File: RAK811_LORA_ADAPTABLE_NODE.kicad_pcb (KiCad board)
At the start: 2 copper layers, 75 x 49 mm, 41 parts, among them J1 Screw_Terminal_01x02, J10 Conn_01x01_Male, J11 Conn_01x01_Male, J12 Conn_01x01_Male, J13 Conn_01x01_Male, J14 Conn_01x01_Male, J15 Conn_01x01_Male, J16 Conn_01x01_Male, J17 Conn_01x01_Male, J18 Conn_01x01_Male, J19 Conn_01x01_Male, J2 Screw_Terminal_01x03, J20 Conn_01x01_Male, J21 Conn_01x01_Male, J22 Conn_01x01_Male, J23 Conn_01x01_Male, J24 Conn_01x01_Male, J25 Conn_01x01_Male, J26 Conn_01x01_Male, J27 Conn_01x01_Male, J28 Conn_01x01_Male, J29 Conn_01x01_Male, J3 Conn_01x01_Male, J30 Conn_01x01_Male, J31 Conn_01x01_Male, J32 Conn_01x01_Male, J4 Conn_01x01_Male, J5 Conn_01x01_Male, J6 Conn_01x01_Male, J7 Conn_Coaxial, J8 Conn_01x01_Male, J9 Conn_01x01_Male, U1 RAK811-HF

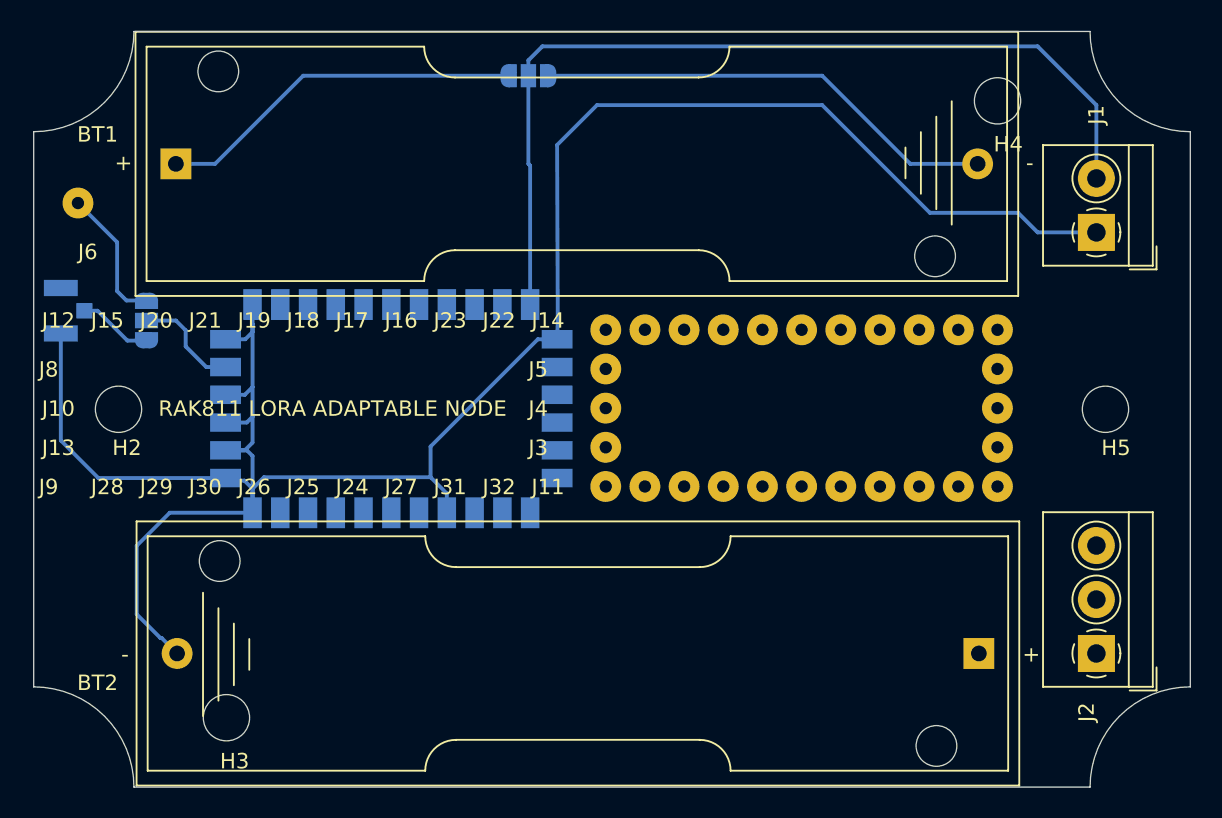
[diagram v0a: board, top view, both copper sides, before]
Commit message: 3 of 4 i/o connectors changed from individual to row
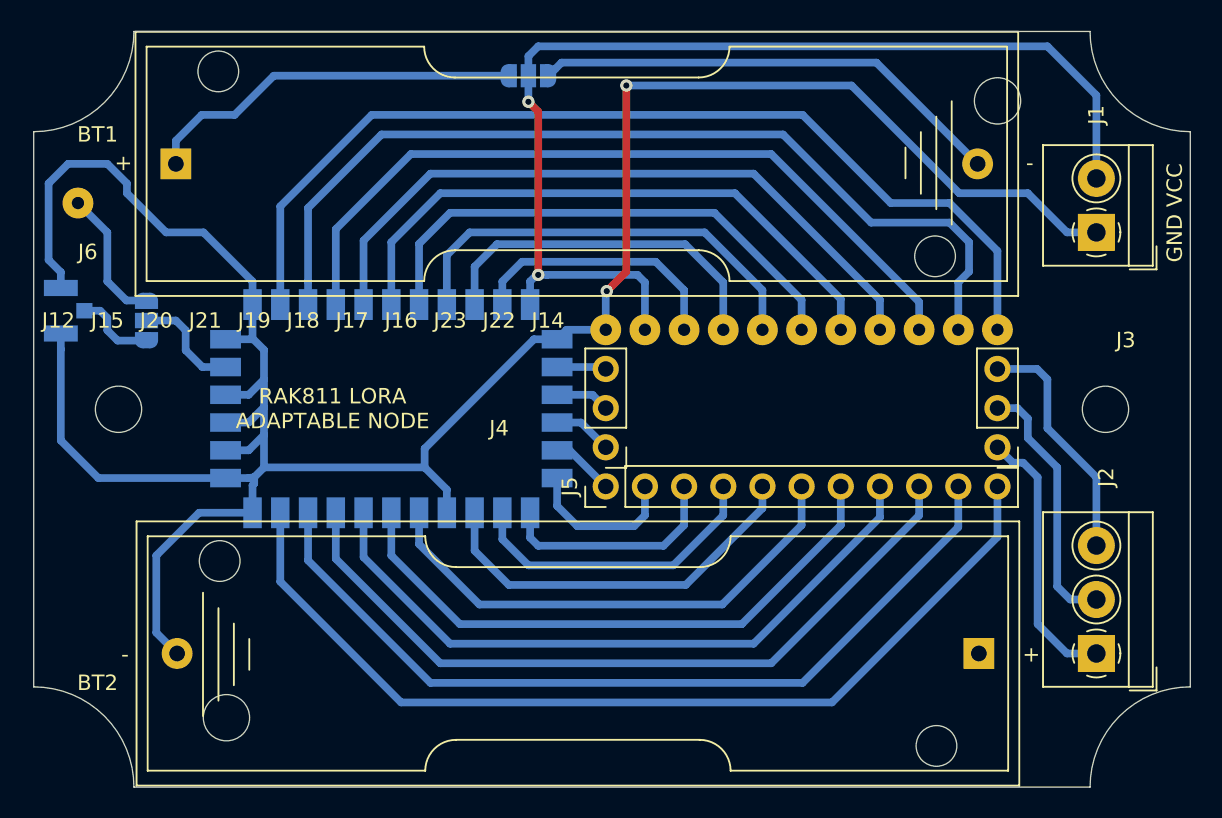
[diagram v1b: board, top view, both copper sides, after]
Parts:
- removed J10, J11, J13, J24, J25, J26, J27, J28, J29, J30, J31, J32, J8, J9: Conn_01x01_Male, Connector_Wire:SolderWirePad_1x01_Drill0.8mm
- J3, J4: value Conn_01x01_Male -> Conn_01x03_Male; footprint Connector_Wire:SolderWirePad_1x01_Drill0.8mm -> Connector_PinHeader_2.54mm:PinHeader_1x03_P2.54mm_Vertical
- J5: value Conn_01x01_Male -> Conn_01x11_Male; footprint Connector_Wire:SolderWirePad_1x01_Drill0.8mm -> Connector_PinHeader_2.54mm:PinHeader_1x11_P2.54mm_Vertical
- moved J5 26.5 mm to (137.1, 129.5), turned to 90 degrees
- moved J4 25.5 mm to (137.1, 127.0), turned to 180 degrees
- turned J3 to 180 degrees
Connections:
- J4 pad 1: Net-(J2-Pad2) -> Net-(J4-Pad1)
- J5 pad 1: Net-(J2-Pad3) -> Net-(J5-Pad1)
- U1 pad 13: Net-(J8-Pad1) -> Net-(J4-Pad3)
- U1 pad 14: Net-(J10-Pad1) -> Net-(J4-Pad2)
- U1 pad 15: Net-(J13-Pad1) -> Net-(J4-Pad1)
- U1 pad 16: Net-(J9-Pad1) -> Net-(J5-Pad1)
- U1 pad 17: Net-(J28-Pad1) -> Net-(J5-Pad2)
- U1 pad 18: Net-(J29-Pad1) -> Net-(J5-Pad3)
- U1 pad 19: Net-(J30-Pad1) -> Net-(J5-Pad4)
- U1 pad 20: Net-(J26-Pad1) -> Net-(J5-Pad5)
- U1 pad 22: Net-(J25-Pad1) -> Net-(J5-Pad6)
- U1 pad 23: Net-(J24-Pad1) -> Net-(J5-Pad7)
- U1 pad 24: Net-(J27-Pad1) -> Net-(J5-Pad8)
- U1 pad 25: Net-(J31-Pad1) -> Net-(J5-Pad9)
- U1 pad 26: Net-(J32-Pad1) -> Net-(J5-Pad10)
- U1 pad 27: Net-(J11-Pad1) -> Net-(J5-Pad11)
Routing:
- net Net-(J14-Pad1): track 0.00 -> 64.1 mm
- net Net-(J5-Pad11): track 0.00 -> 61.9 mm
- net Net-(J22-Pad1): track 0.00 -> 60.0 mm
- net Net-(J5-Pad10): track 0.00 -> 55.4 mm
- net Net-(J23-Pad1): track 0.00 -> 50.5 mm
- net Net-(J5-Pad9): track 0.00 -> 49.5 mm
- net Net-(J16-Pad1): track 0.00 -> 44.8 mm
- net Net-(J5-Pad8): track 0.00 -> 44.1 mm
- net Net-(J17-Pad1): track 0.00 -> 39.3 mm
- net Net-(J5-Pad7): track 0.00 -> 38.9 mm
- net Net-(J18-Pad1): track 0.00 -> 33.9 mm
- net Net-(J5-Pad6): track 0.00 -> 33.1 mm
- net Net-(J19-Pad1): track 0.00 -> 28.4 mm
- net Net-(BT2-Pad2): track 141.3 -> 168.6 mm, vias 0 -> 2
- net Net-(J5-Pad5): track 0.00 -> 25.5 mm
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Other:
- net class Default: trace_width 0.25 -> 0.5
- board text added: "GND VCC"
- board text added: "JP1 BATT 1-2 BT1+BT2 2-3 BT2"
- board text added: "JP2 ANT 1-2 J6 2-3 U.FL"

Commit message: all i/o routed, some battery fine tuning traces todo
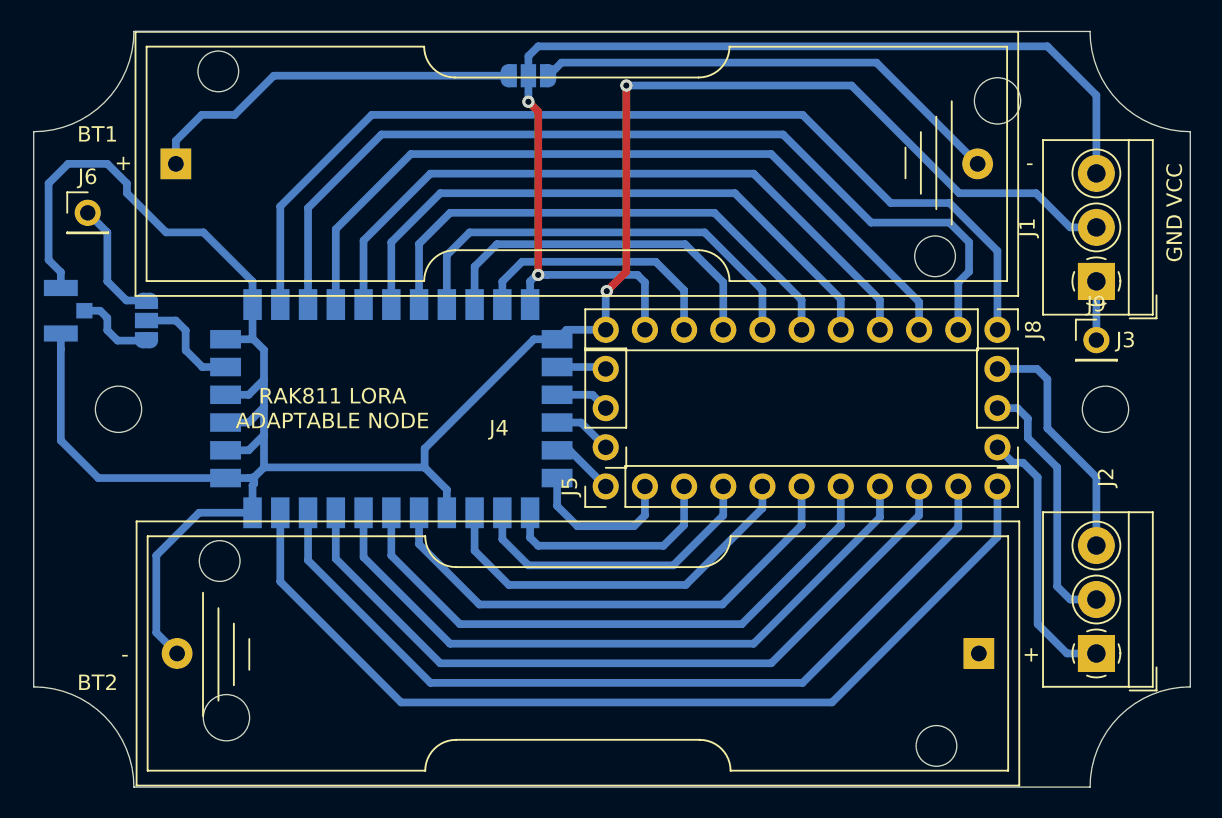
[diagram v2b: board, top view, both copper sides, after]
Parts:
- removed J12, J14, J15, J16, J17, J18, J19, J20, J21, J22, J23: Conn_01x01_Male, Connector_Wire:SolderWirePad_1x01_Drill0.8mm
- added J8: Conn_01x11_Male, Connector_PinHeader_2.54mm:PinHeader_1x11_P2.54mm_Vertical, F.Cu at (162.5, 119.3)
- added J9: Conn_01x01_Male, Connector_PinHeader_2.54mm:PinHeader_1x01_P2.54mm_Vertical, F.Cu at (168.9, 120.0)
- J1: value Screw_Terminal_01x02 -> Screw_Terminal_01x03; footprint TerminalBlock_4Ucon:TerminalBlock_4Ucon_1x02_P3.50mm_Horizontal -> TerminalBlock_4Ucon:TerminalBlock_4Ucon_1x03_P3.50mm_Horizontal
- J6: footprint Connector_Wire:SolderWirePad_1x01_Drill0.8mm -> Connector_PinHeader_2.54mm:PinHeader_1x01_P2.54mm_Vertical
- moved J1 3.17 mm to (168.9, 116.2)
- moved J6 0.90 mm to (103.5, 111.8)
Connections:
- J1 pad 1: Net-(BT2-Pad2) -> Net-(J1-Pad1)
- J1 pad 2: Net-(J1-Pad2) -> Net-(BT2-Pad2)
- JP1 pad 2: Net-(J1-Pad2) -> Net-(J1-Pad3)
- U1 pad 11: Net-(J1-Pad2) -> Net-(J1-Pad3)
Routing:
- net Net-(J1-Pad2): track 71.0 -> 0.00 mm, vias 2 -> 0
- net Net-(J1-Pad3): track 0.00 -> 70.7 mm, vias 0 -> 2
- net Net-(J1-Pad1): track 0.00 -> 3.81 mm
- net Net-(BT2-Pad2): track 168.6 -> 167.0 mm
- net Net-(J6-Pad1): track 8.92 -> 8.02 mm

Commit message: all traces routed
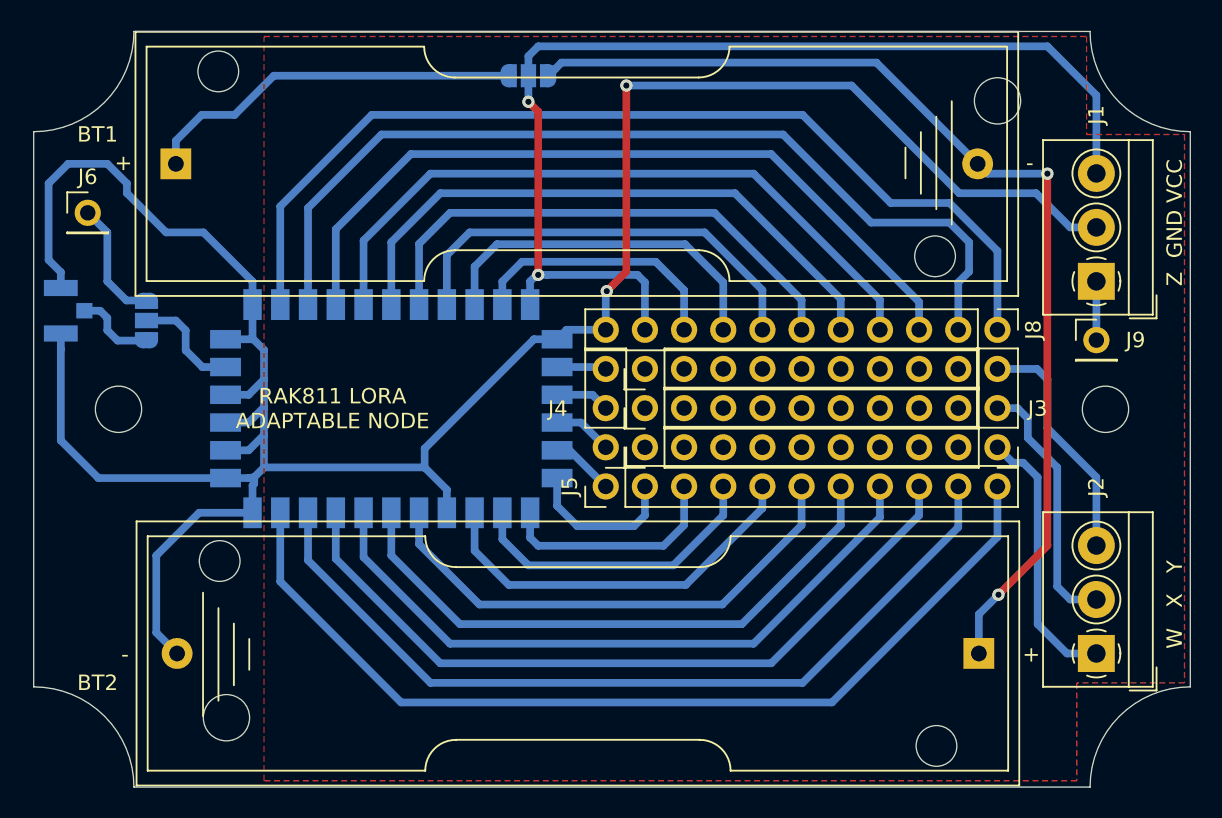
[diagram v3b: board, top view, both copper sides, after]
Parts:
- added J10: Conn_01x09_Male, Connector_PinHeader_2.54mm:PinHeader_1x09_P2.54mm_Vertical, F.Cu at (139.6, 127.0)
- added J11: Conn_01x09_Male, Connector_PinHeader_2.54mm:PinHeader_1x09_P2.54mm_Vertical, F.Cu at (139.6, 124.4)
- added J12: Conn_01x09_Male, Connector_PinHeader_2.54mm:PinHeader_1x09_P2.54mm_Vertical, F.Cu at (139.6, 121.9)
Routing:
- net Net-(BT1-Pad2): track 30.9 -> 68.6 mm, vias 0 -> 2
- added copper zone on F.Cu, net Net-(BT2-Pad2)
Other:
- board text added: "W X Y"
- board text added: "Z GND VCC"
- board text removed: "GND VCC"

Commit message: osw logo
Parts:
- added REF**: OSHW-Symbol_6.7x6mm_Copper, Symbol:OSHW-Symbol_6.7x6mm_Copper, F.Cu at (128.9, 123.8)
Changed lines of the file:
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@@
     (tracks 247)
     (zones 0)
-    (modules 21)
+    (modules 22)
     (nets 62)
   )
@@
     (add_net "Net-(JP2-Pad2)")
   )
+  (module Symbol:OSHW-Symbol_6.7x6mm_Copper (layer F.Cu)
+    (at 128.905 123.825)
+    (descr "Open Source Hardware Symbol")
+    (tags "Logo Symbol OSHW")
+    (attr virtual)
+    (fp_text reference REF** (at 0 0) (layer F.SilkS) hide
+      (effects (font (size 1 1) (thickness 0.15)))
+    )
+    (fp_text value OSHW-Symbol_6.7x6mm_Copper (at 0.75 0) (layer F.Fab) hide
+      (effects (font (size 1 1) (thickness 0.15)))
+    )
+    (fp_poly (pts (xy 0.555814 -2.531069) (xy 0.639635 -2.086445) (xy 0.94892 -1.958947) (xy 1.258206 -1.831449)
+      (xy 1.629246 -2.083754) (xy 1.733157 -2.154004) (xy 1.827087 -2.216728) (xy 1.906652 -2.269062)
+      (xy 1.96747 -2.308143) (xy 2.005157 -2.331107) (xy 2.015421 -2.336058) (xy 2.03391 -2.323324)
+      (xy 2.07342 -2.288118) (xy 2.129522 -2.234938) (xy 2.197787 -2.168282) (xy 2.273786 -2.092646)
+      (xy 2.353092 -2.012528) (xy 2.431275 -1.932426) (xy 2.503907 -1.856836) (xy 2.566559 -1.790255)
+      (xy 2.614803 -1.737182) (xy 2.64421 -1.702113) (xy 2.651241 -1.690377) (xy 2.641123 -1.66874)
+      (xy 2.612759 -1.621338) (xy 2.569129 -1.552807) (xy 2.513218 -1.467785) (xy 2.448006 -1.370907)
+      (xy 2.410219 -1.31565) (xy 2.341343 -1.214752) (xy 2.28014 -1.123701) (xy 2.229578 -1.04703)
+      (xy 2.192628 -0.989272) (xy 2.172258 -0.954957) (xy 2.169197 -0.947746) (xy 2.176136 -0.927252)
+      (xy 2.195051 -0.879487) (xy 2.223087 -0.811168) (xy 2.257391 -0.729011) (xy 2.295109 -0.63973)
+      (xy 2.333387 -0.550042) (xy 2.36937 -0.466662) (xy 2.400206 -0.396306) (xy 2.423039 -0.34569)
+      (xy 2.435017 -0.321529) (xy 2.435724 -0.320578) (xy 2.454531 -0.315964) (xy 2.504618 -0.305672)
+      (xy 2.580793 -0.290713) (xy 2.677865 -0.272099) (xy 2.790643 -0.250841) (xy 2.856442 -0.238582)
+      (xy 2.97695 -0.215638) (xy 3.085797 -0.193805) (xy 3.177476 -0.174278) (xy 3.246481 -0.158252)
+      (xy 3.287304 -0.146921) (xy 3.295511 -0.143326) (xy 3.303548 -0.118994) (xy 3.310033 -0.064041)
+      (xy 3.31497 0.015108) (xy 3.318364 0.112026) (xy 3.320218 0.220287) (xy 3.320538 0.333465)
+      (xy 3.319327 0.445135) (xy 3.31659 0.548868) (xy 3.312331 0.638241) (xy 3.306555 0.706826)
+      (xy 3.299267 0.748197) (xy 3.294895 0.75681) (xy 3.268764 0.767133) (xy 3.213393 0.781892)
+      (xy 3.136107 0.799352) (xy 3.04423 0.81778) (xy 3.012158 0.823741) (xy 2.857524 0.852066)
+      (xy 2.735375 0.874876) (xy 2.641673 0.89308) (xy 2.572384 0.907583) (xy 2.523471 0.919292)
+      (xy 2.490897 0.929115) (xy 2.470628 0.937956) (xy 2.458626 0.946724) (xy 2.456947 0.948457)
+      (xy 2.440184 0.976371) (xy 2.414614 1.030695) (xy 2.382788 1.104777) (xy 2.34726 1.191965)
+      (xy 2.310583 1.285608) (xy 2.275311 1.379052) (xy 2.243996 1.465647) (xy 2.219193 1.53874)
+      (xy 2.203454 1.591678) (xy 2.199332 1.617811) (xy 2.199676 1.618726) (xy 2.213641 1.640086)
+      (xy 2.245322 1.687084) (xy 2.291391 1.754827) (xy 2.348518 1.838423) (xy 2.413373 1.932982)
+      (xy 2.431843 1.959854) (xy 2.497699 2.057275) (xy 2.55565 2.146163) (xy 2.602538 2.221412)
+      (xy 2.635207 2.27792) (xy 2.6505 2.310581) (xy 2.651241 2.314593) (xy 2.638392 2.335684)
+      (xy 2.602888 2.377464) (xy 2.549293 2.435445) (xy 2.482171 2.505135) (xy 2.406087 2.582045)
+      (xy 2.325604 2.661683) (xy 2.245287 2.739561) (xy 2.169699 2.811186) (xy 2.103405 2.87207)
+      (xy 2.050969 2.917721) (xy 2.016955 2.94365) (xy 2.007545 2.947883) (xy 1.985643 2.937912)
+      (xy 1.9408 2.91102) (xy 1.880321 2.871736) (xy 1.833789 2.840117) (xy 1.749475 2.782098)
+      (xy 1.649626 2.713784) (xy 1.549473 2.645579) (xy 1.495627 2.609075) (xy 1.313371 2.4858)
+      (xy 1.160381 2.56852) (xy 1.090682 2.604759) (xy 1.031414 2.632926) (xy 0.991311 2.648991)
+      (xy 0.981103 2.651226) (xy 0.968829 2.634722) (xy 0.944613 2.588082) (xy 0.910263 2.515609)
+      (xy 0.867588 2.421606) (xy 0.818394 2.310374) (xy 0.76449 2.186215) (xy 0.707684 2.053432)
+      (xy 0.649782 1.916327) (xy 0.592593 1.779202) (xy 0.537924 1.646358) (xy 0.487584 1.522098)
+      (xy 0.44338 1.410725) (xy 0.407119 1.316539) (xy 0.380609 1.243844) (xy 0.365658 1.196941)
+      (xy 0.363254 1.180833) (xy 0.382311 1.160286) (xy 0.424036 1.126933) (xy 0.479706 1.087702)
+      (xy 0.484378 1.084599) (xy 0.628264 0.969423) (xy 0.744283 0.835053) (xy 0.83143 0.685784)
+      (xy 0.888699 0.525913) (xy 0.915086 0.359737) (xy 0.909585 0.191552) (xy 0.87119 0.025655)
+      (xy 0.798895 -0.133658) (xy 0.777626 -0.168513) (xy 0.666996 -0.309263) (xy 0.536302 -0.422286)
+      (xy 0.390064 -0.506997) (xy 0.232808 -0.562806) (xy 0.069057 -0.589126) (xy -0.096667 -0.58537)
+      (xy -0.259838 -0.55095) (xy -0.415935 -0.485277) (xy -0.560433 -0.387765) (xy -0.605131 -0.348187)
+      (xy -0.718888 -0.224297) (xy -0.801782 -0.093876) (xy -0.858644 0.052315) (xy -0.890313 0.197088)
+      (xy -0.898131 0.35986) (xy -0.872062 0.52344) (xy -0.814755 0.682298) (xy -0.728856 0.830906)
+      (xy -0.617014 0.963735) (xy -0.481877 1.075256) (xy -0.464117 1.087011) (xy -0.40785 1.125508)
+      (xy -0.365077 1.158863) (xy -0.344628 1.18016) (xy -0.344331 1.180833) (xy -0.348721 1.203871)
+      (xy -0.366124 1.256157) (xy -0.394732 1.33339) (xy -0.432735 1.431268) (xy -0.478326 1.545491)
+      (xy -0.529697 1.671758) (xy -0.585038 1.805767) (xy -0.642542 1.943218) (xy -0.700399 2.079808)
+      (xy -0.756802 2.211237) (xy -0.809942 2.333205) (xy -0.85801 2.441409) (xy -0.899199 2.531549)
+      (xy -0.931699 2.599323) (xy -0.953703 2.64043) (xy -0.962564 2.651226) (xy -0.98964 2.642819)
+      (xy -1.040303 2.620272) (xy -1.105817 2.587613) (xy -1.141841 2.56852) (xy -1.294832 2.4858)
+      (xy -1.477088 2.609075) (xy -1.570125 2.672228) (xy -1.671985 2.741727) (xy -1.767438 2.807165)
+      (xy -1.81525 2.840117) (xy -1.882495 2.885273) (xy -1.939436 2.921057) (xy -1.978646 2.942938)
+      (xy -1.991381 2.947563) (xy -2.009917 2.935085) (xy -2.050941 2.900252) (xy -2.110475 2.846678)
+      (xy -2.184542 2.777983) (xy -2.269165 2.697781) (xy -2.322685 2.646286) (xy -2.416319 2.554286)
+      (xy -2.497241 2.471999) (xy -2.562177 2.402945) (xy -2.607858 2.350644) (xy -2.631011 2.318616)
+      (xy -2.633232 2.312116) (xy -2.622924 2.287394) (xy -2.594439 2.237405) (xy -2.550937 2.167212)
+      (xy -2.495577 2.081875) (xy -2.43152 1.986456) (xy -2.413303 1.959854) (xy -2.346927 1.863167)
+      (xy -2.287378 1.776117) (xy -2.237984 1.703595) (xy -2.202075 1.650493) (xy -2.182981 1.621703)
+      (xy -2.181136 1.618726) (xy -2.183895 1.595782) (xy -2.198538 1.545336) (xy -2.222513 1.474041)
+      (xy -2.253266 1.388547) (xy -2.288244 1.295507) (xy -2.324893 1.201574) (xy -2.360661 1.113399)
+      (xy -2.392994 1.037634) (xy -2.419338 0.980931) (xy -2.437142 0.949943) (xy -2.438407 0.948457)
+      (xy -2.449294 0.939601) (xy -2.467682 0.930843) (xy -2.497606 0.921277) (xy -2.543103 0.909996)
+      (xy -2.608209 0.896093) (xy -2.696961 0.878663) (xy -2.813393 0.856798) (xy -2.961542 0.829591)
+      (xy -2.993618 0.823741) (xy -3.088686 0.805374) (xy -3.171565 0.787405) (xy -3.23493 0.771569)
+      (xy -3.271458 0.7596) (xy -3.276356 0.75681) (xy -3.284427 0.732072) (xy -3.290987 0.67679)
+      (xy -3.296033 0.597389) (xy -3.299559 0.500296) (xy -3.301561 0.391938) (xy -3.302036 0.27874)
+      (xy -3.300977 0.167128) (xy -3.298382 0.063529) (xy -3.294246 -0.025632) (xy -3.288563 -0.093928)
+      (xy -3.281331 -0.134934) (xy -3.276971 -0.143326) (xy -3.252698 -0.151792) (xy -3.197426 -0.165565)
+      (xy -3.116662 -0.18345) (xy -3.015912 -0.204252) (xy -2.900683 -0.226777) (xy -2.837902 -0.238582)
+      (xy -2.718787 -0.260849) (xy -2.612565 -0.281021) (xy -2.524427 -0.298085) (xy -2.459566 -0.311031)
+      (xy -2.423174 -0.318845) (xy -2.417184 -0.320578) (xy -2.407061 -0.34011) (xy -2.385662 -0.387157)
+      (xy -2.355839 -0.454997) (xy -2.320445 -0.536909) (xy -2.282332 -0.626172) (xy -2.244353 -0.716065)
+      (xy -2.20936 -0.799865) (xy -2.180206 -0.870853) (xy -2.159743 -0.922306) (xy -2.150823 -0.947503)
+      (xy -2.150657 -0.948604) (xy -2.160769 -0.968481) (xy -2.189117 -1.014223) (xy -2.232723 -1.081283)
+      (xy -2.288606 -1.165116) (xy -2.353787 -1.261174) (xy -2.391679 -1.31635) (xy -2.460725 -1.417519)
+      (xy -2.52205 -1.50937) (xy -2.572663 -1.587256) (xy -2.609571 -1.646531) (xy -2.629782 -1.682549)
+      (xy -2.632701 -1.690623) (xy -2.620153 -1.709416) (xy -2.585463 -1.749543) (xy -2.533063 -1.806507)
+      (xy -2.467384 -1.875815) (xy -2.392856 -1.952969) (xy -2.313913 -2.033475) (xy -2.234983 -2.112837)
+      (xy -2.1605 -2.18656) (xy -2.094894 -2.250148) (xy -2.042596 -2.299106) (xy -2.008039 -2.328939)
+      (xy -1.996478 -2.336058) (xy -1.977654 -2.326047) (xy -1.932631 -2.297922) (xy -1.865787 -2.254546)
+      (xy -1.781499 -2.198782) (xy -1.684144 -2.133494) (xy -1.610707 -2.083754) (xy -1.239667 -1.831449)
+      (xy -0.621095 -2.086445) (xy -0.537275 -2.531069) (xy -0.453454 -2.975693) (xy 0.471994 -2.975693)
+      (xy 0.555814 -2.531069)) (layer F.Cu) (width 0.01))
+  )
   (module Connector_PinHeader_2.54mm:PinHeader_1x09_P2.54mm_Vertical (layer F.Cu)
     (at 139.635 121.885 90)
@@
     (effects (font (size 1 1) (thickness 0.15)) (justify left mirror))
   )
-  (gr_text "RAK811 LORA \nADAPTABLE NODE" (at 119.38 124.46) (layer F.SilkS)
+  (gr_text "RAK811 LORA \nADAPTABLE NODE" (at 118.745 123.825) (layer F.SilkS)
     (effects (font (size 1 1) (thickness 0.15)))
   )

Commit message: Z external connector pad aligned to expansion area connectors
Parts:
- added REF**: OSHW-Symbol_6.7x6mm_SilkScreen, Symbol:OSHW-Symbol_6.7x6mm_SilkScreen, B.Cu at (137.8, 140.3)
- moved J9 3.93 mm to (165.0, 119.3)
- moved J1 0.80 mm to (168.9, 115.4)
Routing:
- net Net-(J1-Pad1): track 3.81 -> 6.72 mm
- net Net-(BT1-Pad2): track 68.6 -> 69.9 mm
- net Net-(J1-Pad3): track 70.7 -> 69.9 mm
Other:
- board text added: "RAK811 LORA ADAPTABLE NODE V 0"
- board text removed: "RAK811 LORA ADAPTABLE NODE"
